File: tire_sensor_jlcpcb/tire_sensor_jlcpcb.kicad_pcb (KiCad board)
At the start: 4 copper layers, 33 x 26 mm, 37 parts, among them J1 Conn_02x05_Odd_Even, U2 DPS368, U3 LSM6DS3, X1 NX2016SA-32MHZ-EXS00A-CS06654, X2 32.768kHz

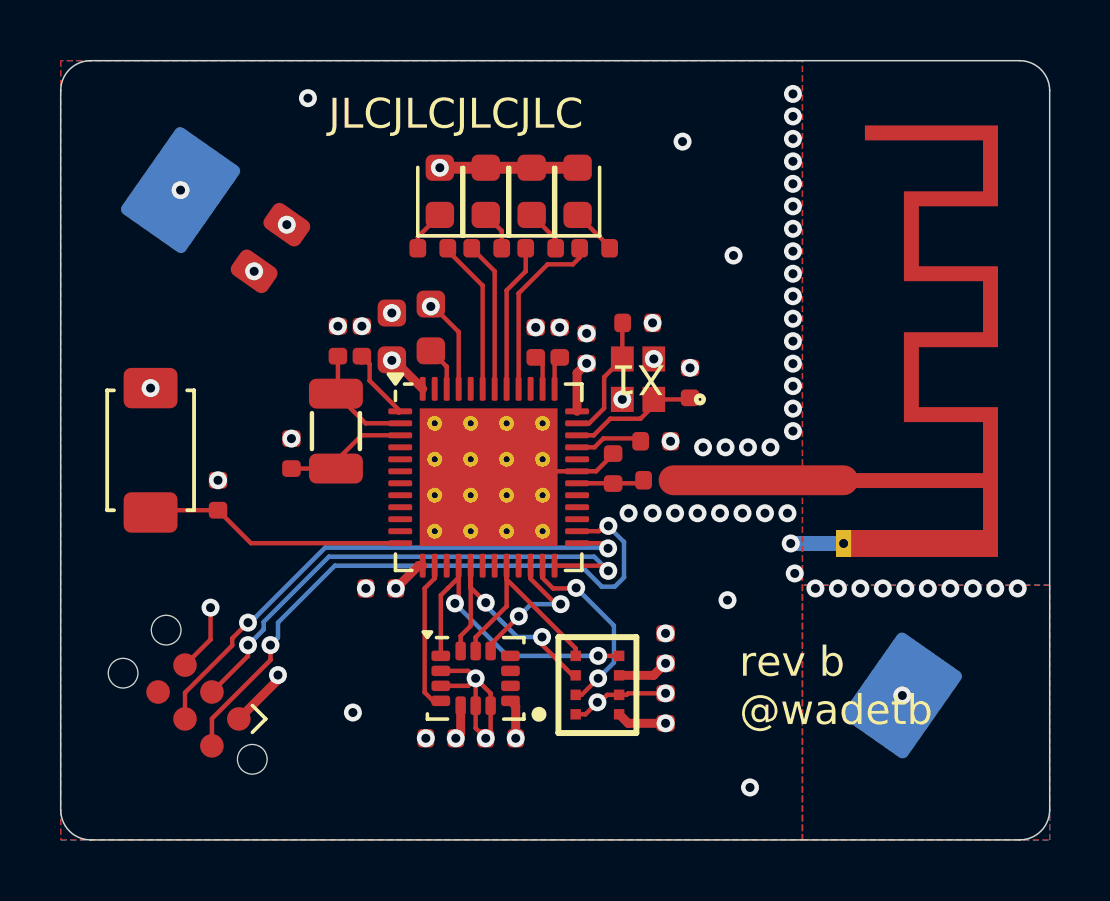
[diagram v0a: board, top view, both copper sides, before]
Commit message: Swap crystal to FA-128 and regen fab outputs
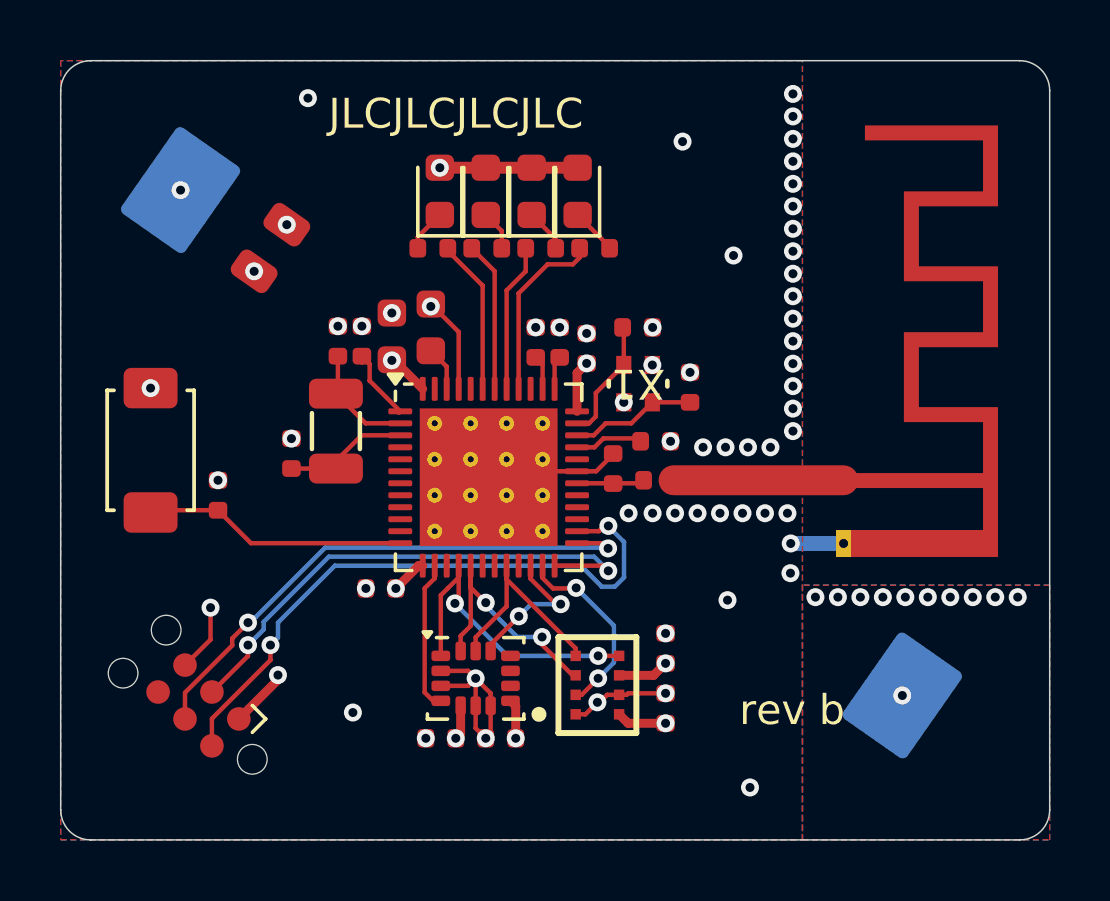
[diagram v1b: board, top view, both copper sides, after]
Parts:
- X1: footprint footprints:NX2016SA_NDK -> footprints:FA-128_EPS
- moved X1 0.15 mm to (175.1, 102.7)
- moved C1 0.15 mm to (176.8, 102.8)
- moved C2 0.15 mm to (175.1, 100.8)
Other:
- board text added: "rev b"
- board text removed: "rev b @wadetb"
